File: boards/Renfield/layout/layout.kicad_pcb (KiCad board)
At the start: 4 copper layers, 37 x 20 mm, 40 parts, among them J1 2060-452/998-404, J2 ?, J3 USB4105-GF-A, Q1 CSD17318Q2, U1 TPS70933QDRVRQ1, U2 STM32G0B1KBU6N, U3 TCPP01-M12

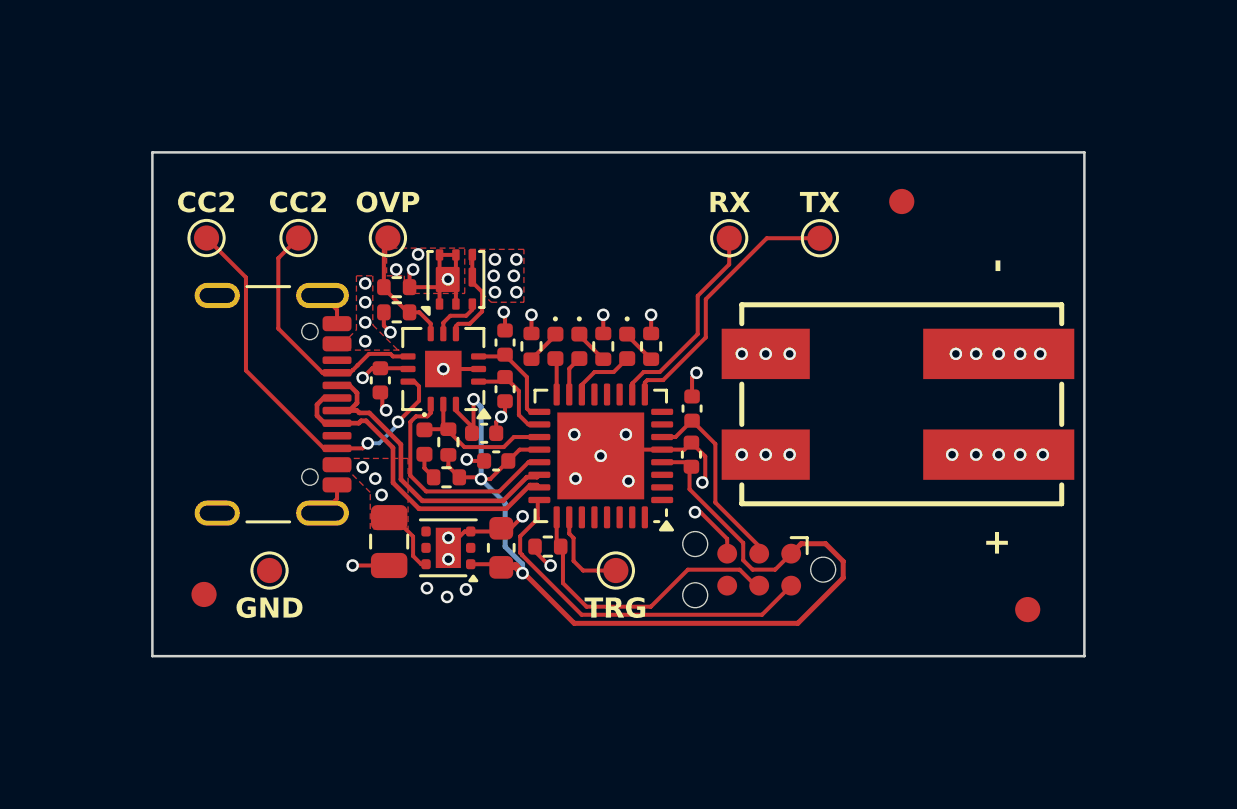
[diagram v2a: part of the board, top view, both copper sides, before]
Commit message: layout(Renfield): layout tweaks + bump Logo to 0.5.1
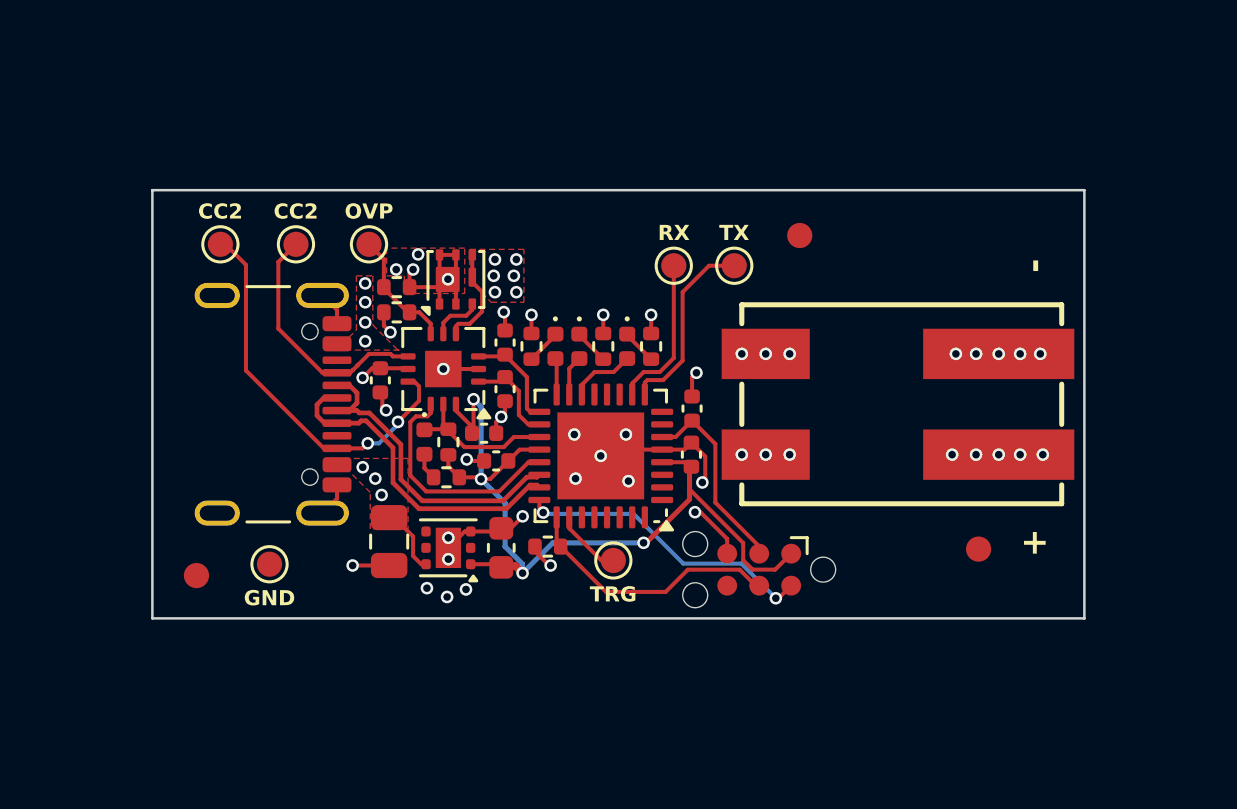
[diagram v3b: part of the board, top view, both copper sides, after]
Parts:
- removed #G1: ?, diodeinc_registry_modules_Logo@0.5.0:diode
- added #LOGO1: ?, diodeinc_registry_modules_Logo@0.5.1:diode, F.Cu at (149.3, 94.5)
- moved FID1 4.27 mm to (157.2, 93.3)
- moved TP7 3.57 mm to (154.6, 94.5)
- moved FID2 3.09 mm to (164.3, 105.8)
- moved TP6 2.46 mm to (152.2, 94.5)
- moved FID3 0.81 mm to (133.2, 106.8)
- moved TP4 0.79 mm to (140.1, 93.7)
- moved TP2 0.60 mm to (134.2, 93.7)
- moved TP5 0.41 mm to (149.8, 106.2)
- moved TP1 0.27 mm to (137.2, 93.7)
- moved TP3 0.25 mm to (136.2, 106.3)
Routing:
- net V3V3: track 43.1 -> 34.8 mm, vias 3 -> 4
- net UART_TX: track 10.7 -> 7.54 mm
- net SWD_SWDIO: track 14.7 -> 12.1 mm, vias 0 -> 2
- net UART_RX: track 8.17 -> 6.17 mm
- net SWD_SWCLK: track 11.8 -> 10.5 mm
- net SCOPE_MARKER: track 3.64 -> 2.72 mm
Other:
- board size 37 x 20 mm -> 37 x 17 mm

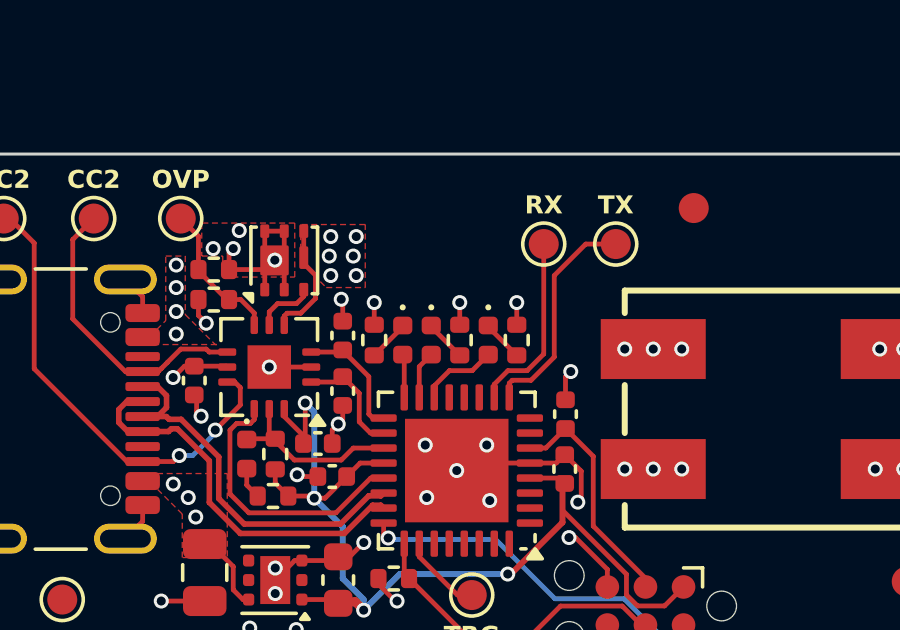
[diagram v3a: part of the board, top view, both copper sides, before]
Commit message: feat(Renfield): firmware-gated load rail (default-off)
Add a shunt N-FET (SSM3K15ACT, 30 V Vds, logic-level) that pulls the
main FET's gate to GND by default, keeping VBUS_PROT / WAGO de-energised
until firmware explicitly enables it.

- R_LOAD_EN_PU (10 k\u03a9) pulls the kill-FET gate up to V3V3 so it's
  already on before TCPP01 exits UVLO \u2014 no window where the main
  FET could close without firmware consent.
- LOAD_EN_N routed to MCU PA4 (active-LOW: high/high-Z = off,
  drive low to enable). Reset-default GPIO state (input floating)
  keeps the load off.
- Hardware OVP path is unaffected: TCPP01 still drives FET_GATE
  when Q_KILL is off, and the 22 V OVP backstop still works.

Build: 42 components, US \.04 @ qty 20 (+\/bin/bash.03).
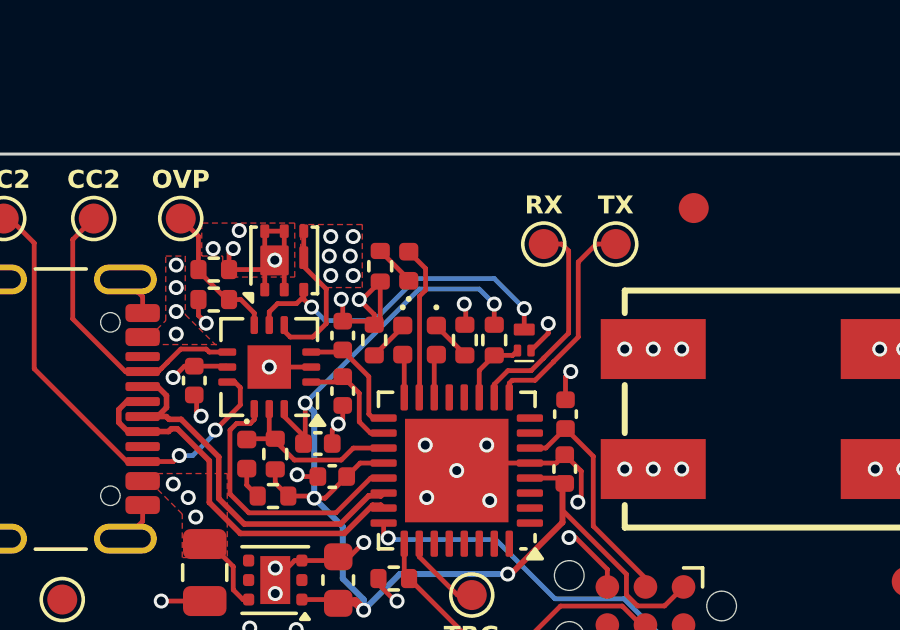
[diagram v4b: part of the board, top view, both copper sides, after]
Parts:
- added Q1: SSM3K15ACT,L3F, diodeinc_registry_components_Toshiba_SSM3KxxxCT@0.1.0:SSM3KxxxCT, F.Cu at (151.6, 97.7)
- added R3: ERJ-2RKF1002X, kicad_libraries_kicad-footprints_Resistor_SMD@9.0.3:R_0402_1005Metric, F.Cu at (150.6, 97.7)
- moved R2 3.62 mm to (146.8, 95.2), turned to -90 degrees
- moved D1 2.57 mm to (147.7, 95.2), turned to 90 degrees
- moved R6 1.73 mm to (149.6, 97.7)
- moved D4 1.73 mm to (148.6, 97.7)
- moved #LOGO1 0.35 mm to (149.7, 94.5)
- renumbered Q1 to Q2, R3 to R4, R4 to R5, R5 to R6, R6 to R7, R7 to R8, R8 to R9
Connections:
- U2 pad 11: U_MCU.PA4 -> LOAD_EN_N
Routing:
- net FET_GATE: track 2.03 -> 11.7 mm, vias 0 -> 2
- net V3V3: track 34.8 -> 43.6 mm, vias 4 -> 5
- net GND: track 25.9 -> 30.1 mm
- net HEARTBEAT_LED: track 1.59 -> 5.18 mm
- net LOAD_EN_N: track 0.00 -> 2.45 mm
- net VBUS_PROT: track 3.99 -> 5.26 mm
- net USB_ENUM_LED: track 2.62 -> 1.47 mm
- net UART_RX: track 6.17 -> 7.29 mm
